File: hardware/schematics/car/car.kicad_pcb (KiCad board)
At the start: 12 copper layers, 17.9 x 30.2 mm, 20 parts, among them M1 Motor_Servo, Q1 PMOS, SW1 SW_SPST, SW2 SW_Push, SW3 SW_Push, U1 VL53L0CXV0DH1, U10 Mini-560, U11 JGA25-37x, U2 VL53L0CXV0DH1, U3 VL53L0CXV0DH1, U4 Pixy2, U6 TB6612FNG, U7 SparkFun OTOS, U9 Mini-360

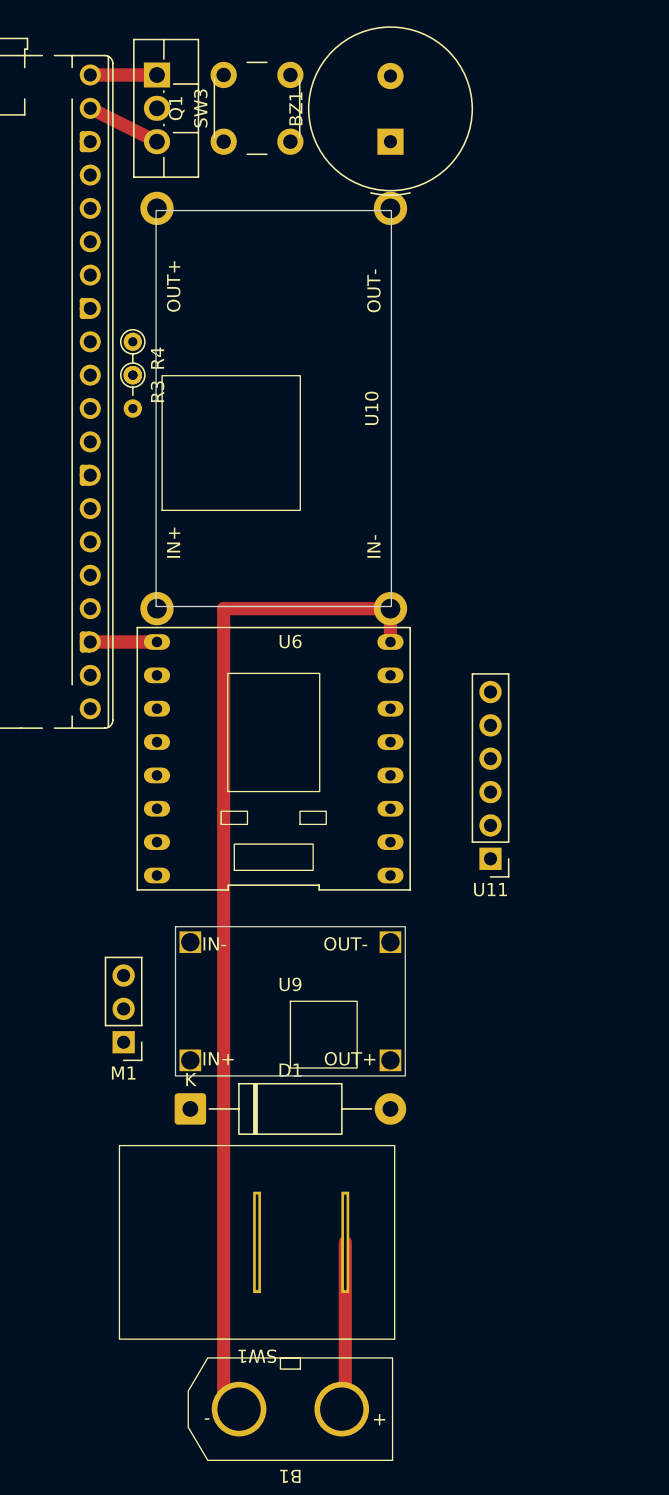
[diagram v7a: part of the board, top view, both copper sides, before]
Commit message: [Schematic] PCB moving again
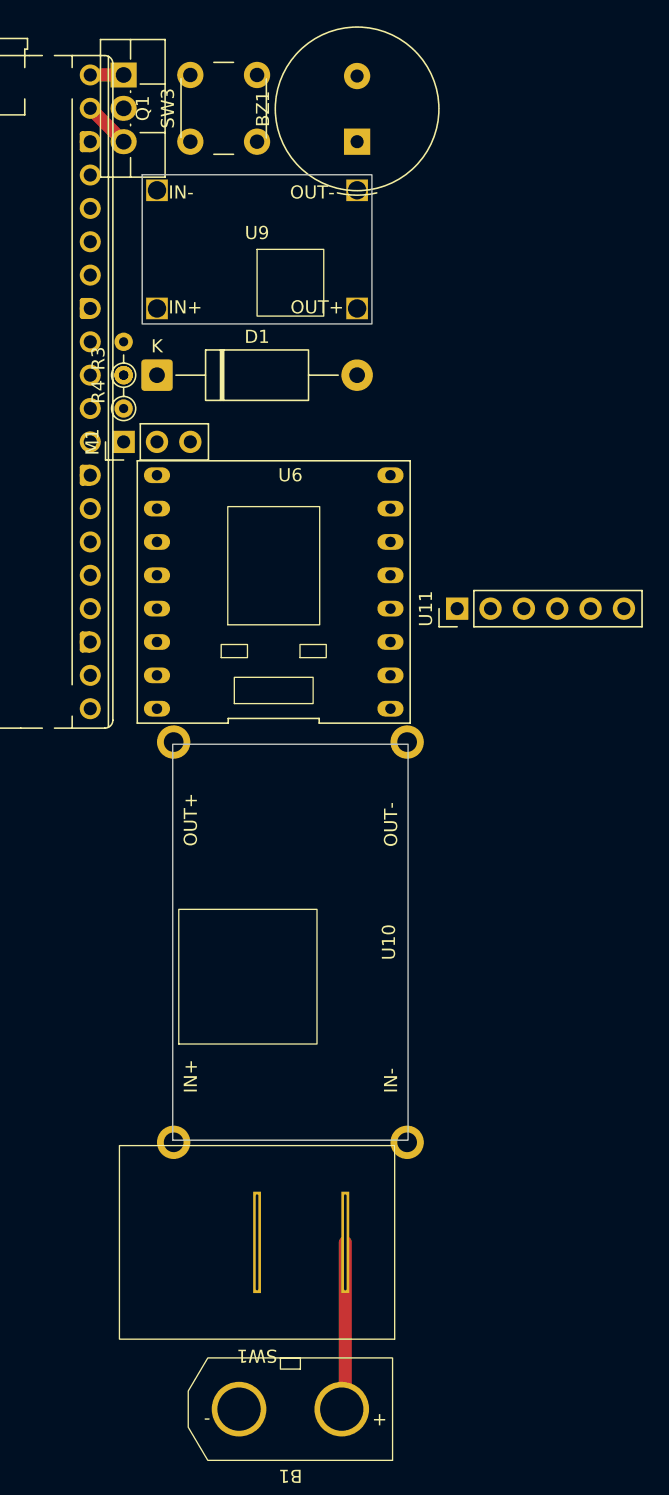
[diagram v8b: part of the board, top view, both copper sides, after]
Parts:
- moved U9 57.3 mm to (157.5, 28.5)
- moved D1 55.9 mm to (149.9, 38.1)
- moved M1 45.7 mm to (147.3, 43.2), turned to 90 degrees
- moved U10 40.7 mm to (160.0, 81.3)
- moved U11 19.2 mm to (172.7, 55.9), turned to 90 degrees
- moved U6 12.7 mm to (158.8, 54.6)
- moved R4 5.13 mm to (147.3, 40.6), turned to 90 degrees
- moved Q1 2.54 mm to (147.3, 15.2)
- moved BZ1 2.54 mm to (165.1, 20.3)
- moved SW3 2.54 mm to (154.9, 17.8)
- moved R3 0.70 mm to (147.3, 38.1), turned to 90 degrees
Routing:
- net GND: track 234.2 -> 152.9 mm
- net +3.3V: track 83.7 -> 30.3 mm
- net Net-(A1-VBUS): track 5.08 -> 2.54 mm
- net Net-(A1-VSYS): track 5.68 -> 3.59 mm
